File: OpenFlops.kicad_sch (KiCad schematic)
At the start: 87 parts, among them P1 FLOPPY_CONN, P10 SD CARD, P11 SD PWR, P12 SD_DISABLE, P2 POWER_INPUT, P3 USB_A_FEMALE, P4 PROG_PORT, P5 JUMPER_JC, P6 ENCODER_PORT, P7 DISPLAY_PORT, P8 USB_HEADER, P9 EXTERNAL_SPEAKER, Q1 BSS138, Q2 BSS138, Q3 BSS138, Q5 BSS138, Q6 BSS138, Q7 MMBT3904, Q8 BSS138, U1 74HCT04, U3 STM32F105RBT6, U4 LM1117MP-3.3, Y1 8 MHz

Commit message: Update jlcpcb part numbers
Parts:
- C1: JLCPCB PN (none) -> C445483; MFG Name (none) -> Nichicon; MFG Part Num (none) -> UCD0J101MCL6GS
- C10, C18, C20, C23, C4, C6, C7, C8, C9: JLCPCB PN CC0805KRX7R9BB104 -> C49678; MFG Part Num MULTILAYER CERAMIC CAPACITORS MLCC - SMD/SMT 100NF 50V 0805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 -> CC0805KRX7R9BB104
- C17, C19: JLCPCB PN (none) -> C445463; MFG Name (none) -> Nichicon; MFG Part Num (none) -> UCD1H100MCL6GS
- C3, C5: JLCPCB PN CL21C220JBANNNC -> C1804; MFG Name SAMSUNG ELECTRO-MECHANICS -> Samsung Electro-Mechanics; MFG Part Num MULTILAYER CERAMIC CAPACITORS MLCC - SMD/SMT 22PF 50V 0805 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 -> CL21C220JBANNNC
- D1, D2: JLCPCB PN 1N4148WS -> C2128; MFG Name CHANGJIANG ELECTRONICS TECH (CJ) -> Jiangsu Changjing Electronics Technology Co., Ltd.; MFG Part Num SWITCHING DIODE 100V 150MA 1.25V @ 150MA 4NS SOD-323 ROHS B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 -> 1N4148WS
- PU1, PU10, PU11, PU12, PU13, PU14, PU15, PU2, PU3, PU4, PU5, PU6, PU7, PU8, PU9, RN1, RN2, RN3, RN4, RN5, RN6: JLCPCB PN 0805W8F1001T5E -> C17513; MFG Name UNIROYAL ELEC -> UNI-ROYAL; MFG Part Num CHIP RESISTOR - SURFACE MOUNT 1KOHMS ±1% 1/8W 0805 ROHS Bas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 -> 0805W8F1001T5E
- Q1, Q2, Q3, Q5, Q6, Q8: JLCPCB PN (none) -> C7420339; MFG Name (none) -> hongjiacheng; MFG Part Num (none) -> BSS138
- Q7: JLCPCB PN MMBT3904 -> C20526; MFG Name CHANGJIANG ELECTRONICS TECH (CJ) -> Jiangsu Changjing Electronics Technology Co., Ltd; MFG Part Num TRANSISTORS (NPN/PNP) NPN 200MA 40V SOT-23(SOT-23-3) ROHS B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 -> MMBT3904(RANGE:100-300)
- R1, R2, R6: JLCPCB PN 0805W8F220JT5E -> C17561; MFG Name UNIROYAL ELEC -> UNI-ROYAL; MFG Part Num CHIP RESISTOR - SURFACE MOUNT 22OHMS ±1% 1/8W 0805 ROHS Bas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 -> 0805W8F220JT5E
- R10, R13, R7: JLCPCB PN 0805W8F4701T5E -> C17673; MFG Name UNIROYAL ELEC -> UNI-ROYAL; MFG Part Num CHIP RESISTOR - SURFACE MOUNT 4.7KOHMS ±1% 1/8W 0805 ROHS -> 0805W8F4701T5E
- R20, R21, R5: JLCPCB PN (none) -> C17513; MFG Name (none) -> UNI-ROYAL; MFG Part Num (none) -> 0805W8F1001T5E
- R3, R4: JLCPCB PN (none) -> C26010; MFG Name (none) -> UNI-ROYAL; MFG Part Num (none) -> 0805W8F3301T5E
- U1: JLCPCB PN 74HCT04D -> C5590; MFG Name NEXPERIA -> Nexperia; MFG Part Num GATES AND INVERTERS SOIC-14_150MIL ROHS Extended Part -> 74HC04D,653
- U3: JLCPCB PN (none) -> C3029577; MFG Name (none) -> ARTERY; MFG Part Num (none) -> AT32F435RGT7
- U4: JLCPCB PN (none) -> C6186; MFG Name (none) -> Advanced Monolithic Systems; MFG Part Num (none) -> AMS1117-3.3
- Y1: JLCPCB PN (none) -> C12674; MFG Name (none) -> YXC Crystal Oscillators; MFG Part Num (none) -> X49SM8MSD2SC

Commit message: Final touches
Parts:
- removed P4: PROG_PORT, Connector_PinHeader_2.54mm:PinHeader_2x05_P2.54mm_Vertical, symbol Connector_Generic:Conn_02x05_Odd_Even
- added P4: PROG_PORT, Connector_PinHeader_2.54mm:PinHeader_2x06_P2.54mm_Vertical, symbol Connector_Generic:Conn_02x06_Odd_Even
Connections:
- net +3.3V: now also P4.12 (Pin_12), P4.9 (Pin_9)
- net +5V: now also P4.6 (Pin_6)
- net GND: now also S3.2, P4.10 (Pin_10), P4.2 (Pin_2), P4.8 (Pin_8); no longer S3.1
- net boot0: now also P4.11 (Pin_11)
- net nrst: now also P4.1 (Pin_1)
- net rx: now also P4.5 (Pin_5)
- net swclk: now also P4.4 (Pin_4)
- net tx: now also P4.7 (Pin_7)
- net at U3.38 (PC7): now also S3.1; no longer S3.2
- net swdio: now reaches U3.46 (PA13)
- net swdio: now also P4.3 (Pin_3)
- no-connect marks 14 -> 12
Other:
- note removed: "RST"

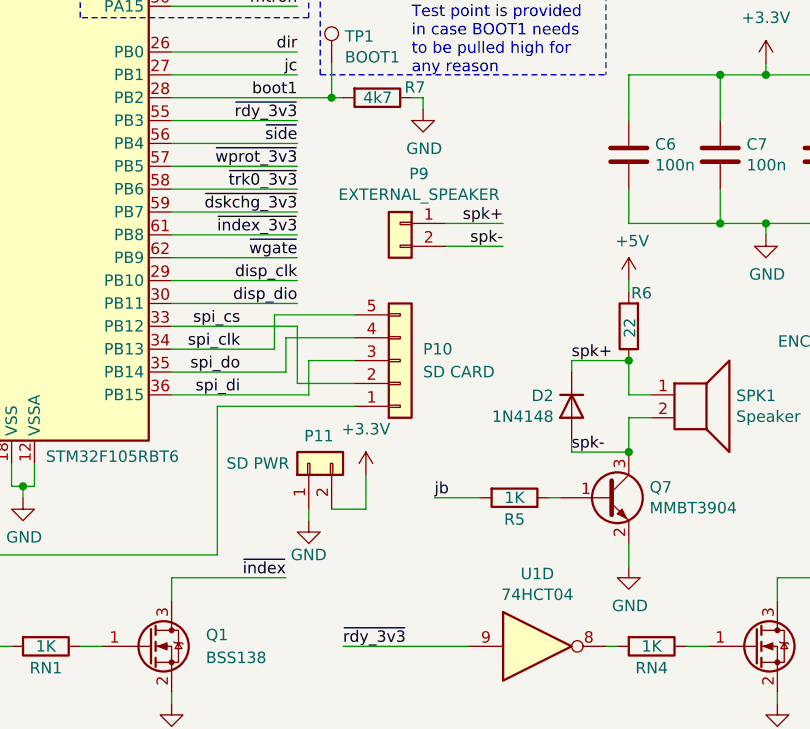
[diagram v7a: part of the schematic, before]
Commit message: Add +5V to SD module connector
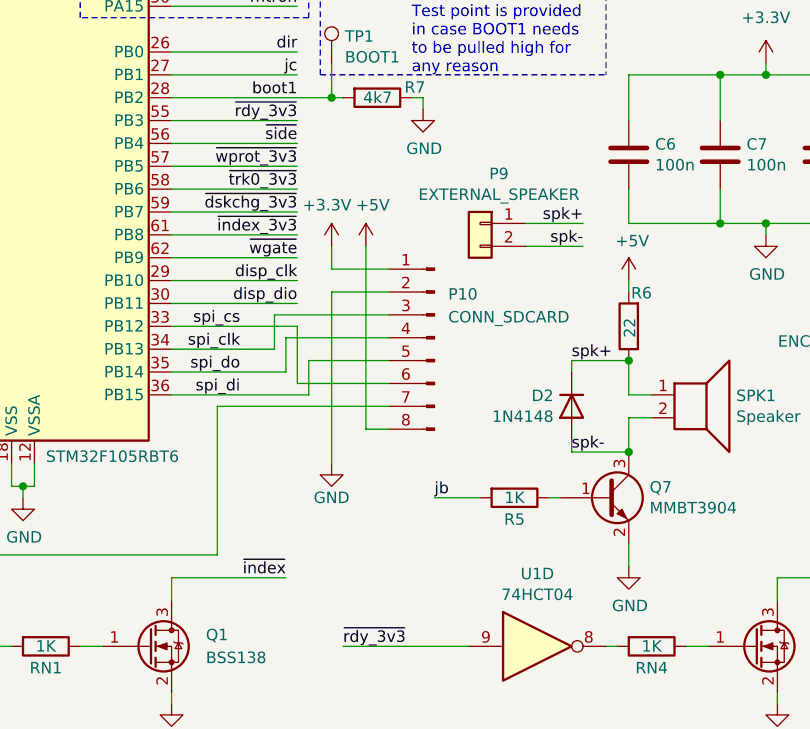
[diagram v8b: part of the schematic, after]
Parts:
- removed P10: SD CARD, Connector_PinHeader_2.54mm:PinHeader_1x05_P2.54mm_Vertical, symbol Connector_Generic:Conn_01x05
- removed P11: SD PWR, Connector_PinHeader_2.54mm:PinHeader_1x02_P2.54mm_Vertical, symbol Connector_Generic:Conn_01x02
- added P10: CONN_SDCARD, Connector_PinHeader_2.54mm:PinHeader_1x08_P2.54mm_Vertical, symbol Connector:Conn_01x08_Pin
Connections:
- net +3.3V: now also P10.1 (Pin_1)
- net +5V: now also P10.8 (Pin_8)
- net GND: now also P10.2 (Pin_2)
- net spi_cd: now also P10.7 (Pin_7)
- net spi_clk: now also P10.3 (Pin_3)
- net spi_cs: now also P10.6 (Pin_6)
- net spi_di: now also P10.5 (Pin_5)
- net spi_do: now also P10.4 (Pin_4)
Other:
- moved on the sheet: P9
